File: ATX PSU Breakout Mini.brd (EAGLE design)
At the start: 100 x 99.8 mm, 43 parts, among them J1 ATX24RH, SW1 SW_PUSH_DPDT, T1 5V, T2 3V3, T3 12V, T4 GND, T5 ADJ, T6 -12V, U1 V_REG_317SINK, U2 TPS2513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

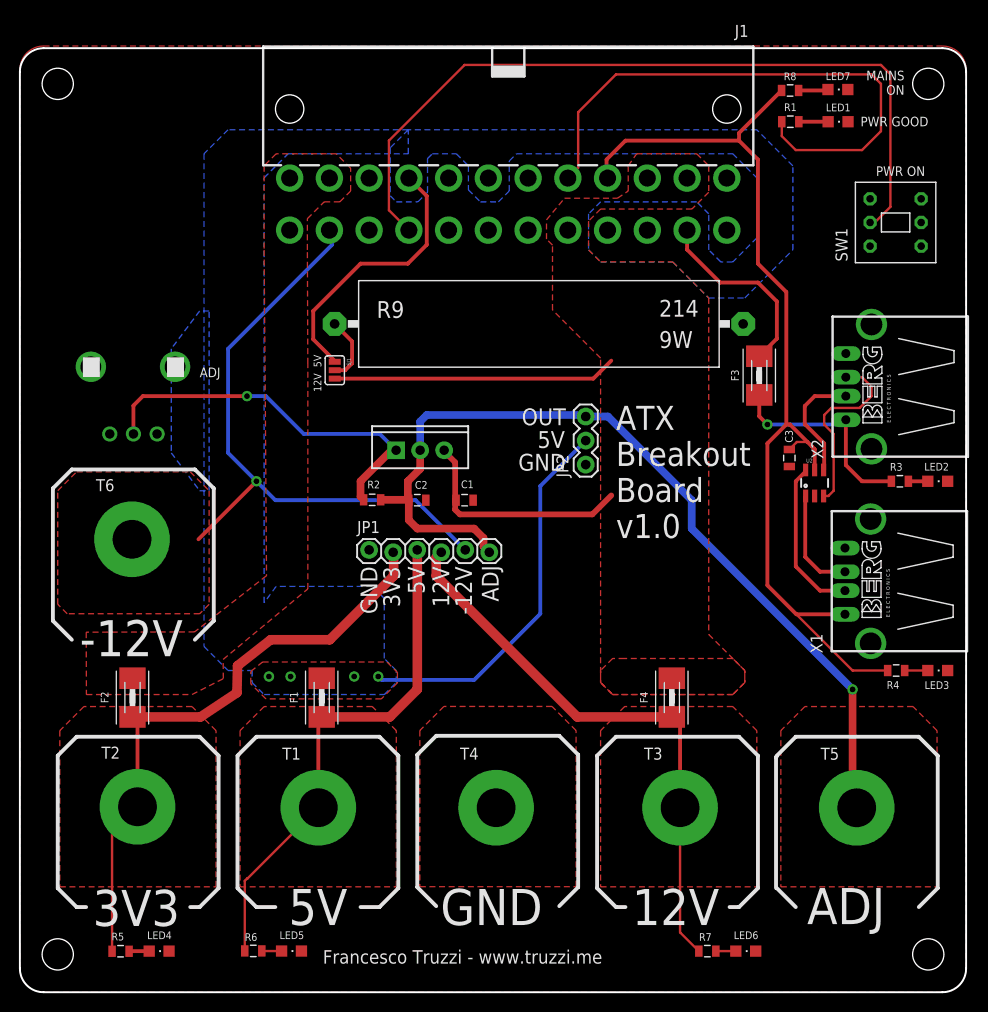
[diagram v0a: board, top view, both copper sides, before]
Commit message: Fixes and additions.
Thickened all traces, added resistors to the USB ports (you can use them
instead of the TPS2513)
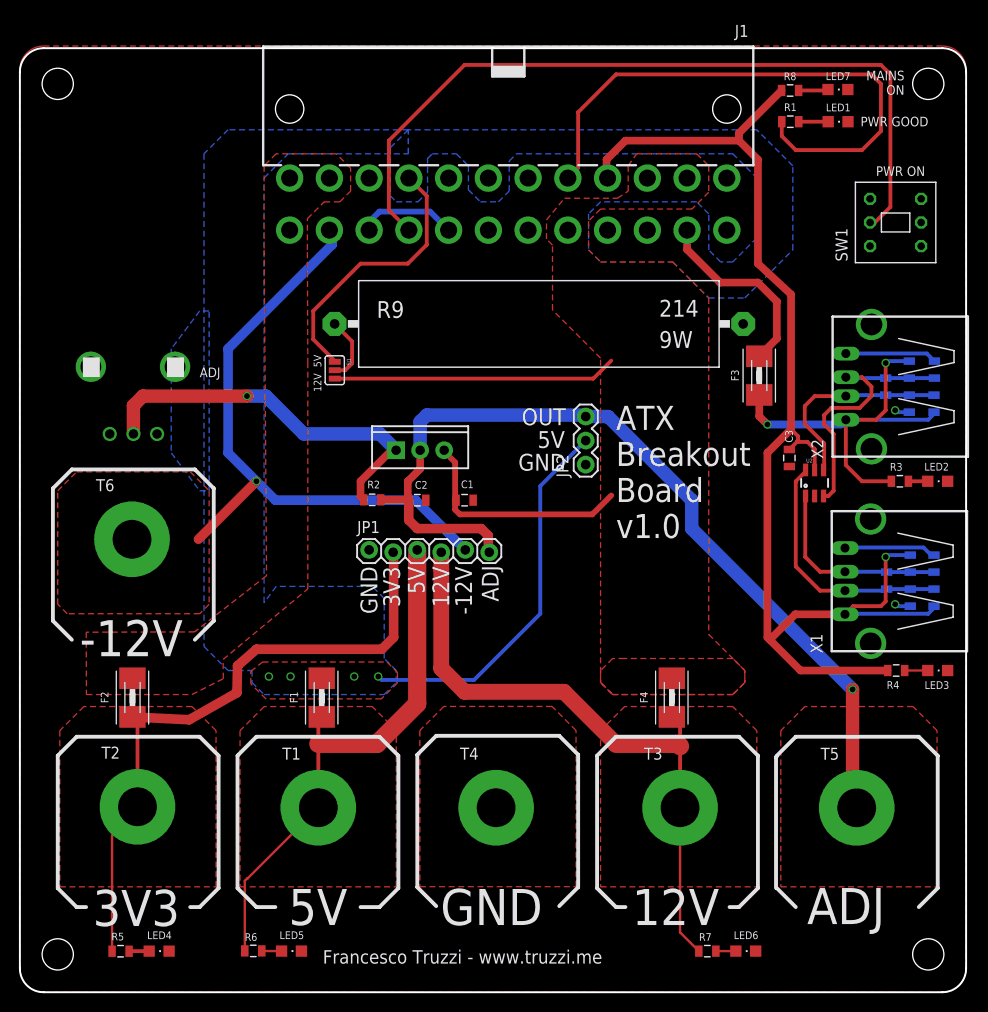
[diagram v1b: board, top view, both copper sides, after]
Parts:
- added R10, R15: (no value), SparkFun-Resistors:0805
- added R11, R16: 43K, SparkFun-Resistors:0805
- added R12, R14, R17, R19: 51K, SparkFun-Resistors:0805
- added R13, R18: 75K, SparkFun-Resistors:0805
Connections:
- net 5V_STDBY: now also R16.1, R18.1
- net DM1: now also R15.1, R16.2, R17.1
- net DM2: now also R10.1, R11.2, R12.1
- net DP1: now also R15.2, R18.2, R19.1
- net DP2: now also R10.2, R13.2, R14.1
- net GND: now also R12.2, R14.2, R17.2, R19.2
- net USB_P4: now also R11.1, R13.1
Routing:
- net GND: track 0.00 -> 33.2 mm, vias 0 -> 2
- net 5V_STDBY: track 104.0 -> 132.5 mm, vias 0 -> 1
- net USB_P4: track 22.3 -> 44.3 mm, vias 1 -> 2
- net DM1: track 16.9 -> 26.4 mm
- net DP1: track 11.3 -> 20.7 mm
- net DP2: track 19.7 -> 29.1 mm
- net DM2: track 12.4 -> 21.8 mm
- net 12VOUT: track 59.7 -> 66.9 mm
- net 3V3OUT: track 63.5 -> 67.4 mm
- net 5VOUT: track 54.2 -> 56.6 mm

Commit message: New version (v1.2)
Fixed bugs, rearranged traces and components, added pin headers, USB
resistors and prototyping area.
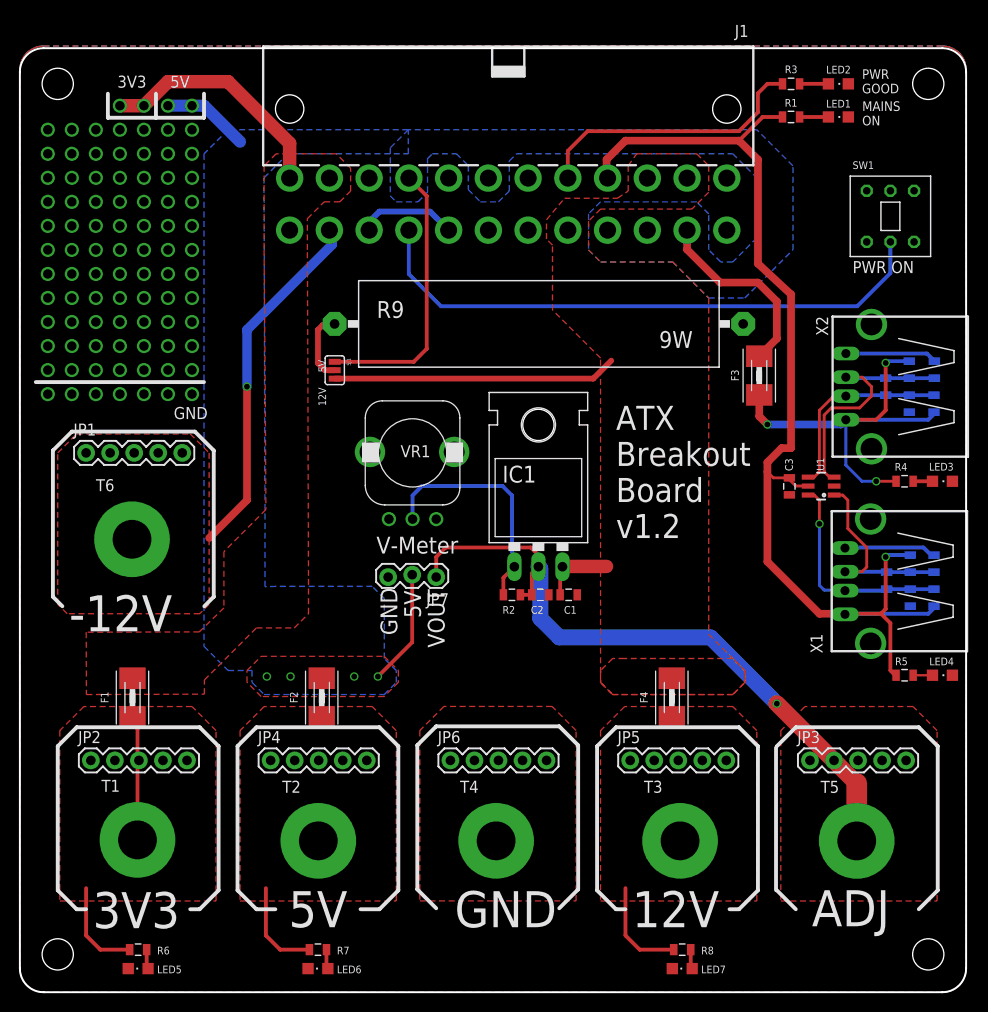
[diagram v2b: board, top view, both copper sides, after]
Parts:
- removed U2: TPS2513, SparkFun-DigitalIC:SOT23-6
- added IC1: (no value), v-reg:317TL
- added JP3, JP4, JP5, JP6: (no value), SparkFun-Connectors:1X05
- added JP7: (no value), SparkFun-Connectors:1X03_LOCK
- JP1: device SparkFun-Connectors:1X06_LOCK -> SparkFun-Connectors:1X05
- JP2: device SparkFun-Connectors:1X03 -> SparkFun-Connectors:1X05
- LED1: value GREEN -> RED
- LED2: value (none) -> GREEN
- LED7: value RED -> (none)
- R10, R15: value (none) -> 43K
- R11, R16: value 43K -> 75K
- R13, R18: value 75K -> (none)
- R3: value 1.2k -> 3.3k
- R6: value 3.3k -> 1.2k
- R7: value 10k -> 3.3k
- R8: value 3.3k -> 10k
- T1: value 5V -> 3V3
- T2: value 3V3 -> 5V
- U1: value V_REG_317SINK -> TPS2513; device SparkFun-PowerIC:TO220-ADJ -> SparkFun-DigitalIC:SOT23-6
- moved LED7 94.3 mm to (48.0, -31.5), turned to 90 degrees
- moved R8 91.5 mm to (48.0, -29.5)
- moved R5 87.8 mm to (71.5, -0.50)
- moved LED4 87.8 mm to (75.5, -0.50)
- moved JP2 60.9 mm to (-14.5, -9.50), turned to 0 degrees
- moved LED6 45.3 mm to (9.50, -31.5), turned to 90 degrees
- moved R3 43.5 mm to (59.5, 62.0)
- moved LED2 43.3 mm to (64.5, 62.0)
- moved U1 42.5 mm to (62.7, 19.5), turned to 90 degrees
- moved R7 41.2 mm to (9.50, -29.5)
- moved JP1 31.6 mm to (-15.0, 23.0)
- moved VR1 30.8 mm to (19.5, 20.0)
- moved R16 24.2 mm to (72.0, 31.8), turned to 270 degrees
- moved R10 22.9 mm to (74.6, 7.70)
- moved R13 22.4 mm to (69.6, 9.50), turned to 90 degrees
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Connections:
- net -12V: now also JP1.1, JP1.2, JP1.3, JP1.4
- net 12V: now also IC1.3; no longer U1.IN
- net 12VOUT: now also JP5.1, JP5.2, JP5.3, JP5.4, JP5.5, R8.1; no longer JP1.4, R7.1
- net 3V3: now also F1.2; no longer F2.2
- net 3V3OUT: now also F1.1, JP2.1, JP2.2, JP2.3, JP2.4, JP2.5, R6.1, T1.P; no longer F2.1, JP1.2, R5.1, T2.P
- net 5V: now also F2.2, JP7.2; no longer F1.2, JP2.2
- net 5VOUT: now also F2.1, JP4.1, JP4.2, JP4.3, JP4.4, JP4.5, R7.1, T2.P; no longer F1.1, JP1.3, R6.1, T1.P
- net 5V_STDBY: now also R1.1, R10.1, R11.1, R5.1, U1.5; no longer R16.1, R18.1, R4.1, R8.1, U2.5
- net DM1: now also R10.2, R12.1, R13.1, U1.6; no longer R15.1, R16.2, R17.1, U2.6
- net DM2: now also R15.2, R17.1, R18.1, U1.4; no longer R10.1, R11.2, R12.1, U2.4
- net DP1: now also R11.2, R13.2, R14.1, U1.1; no longer R15.2, R18.2, R19.1, U2.1
- net DP2: now also R16.2, R18.2, R19.1, U1.3; no longer R10.2, R13.2, R14.1, U2.3
- net GND: now also JP6.1, JP6.2, JP6.3, JP6.4, JP6.5, JP7.3, U1.2; no longer JP1.1, JP2.1, U2.2
- net N$1: now also R3.1; no longer R1.1
- net N$9: now also IC1.1; no longer U1.ADJ
- net USB_P4: now also R15.1, R16.1, R4.1; no longer R11.1, R13.1, R3.1
- net VOUT: now also IC1.2, JP3.1, JP3.2, JP3.3, JP3.4, JP3.5, JP7.1; no longer JP1.6, JP2.3, U1.OUT
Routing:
- net 12VOUT: track 66.9 -> 10.7 mm
- net 5VOUT: track 56.6 -> 10.2 mm
- net 3V3OUT: track 67.4 -> 23.4 mm
- net N$1: track 59.9 -> 29.7 mm
- net -12V: track 66.2 -> 38.0 mm
- net VOUT: track 97.4 -> 71.8 mm
- net 3V3: track 0.00 -> 25.4 mm, vias 0 -> 2
- net N$10: track 83.9 -> 61.7 mm
- net 5V: track 89.9 -> 70.9 mm, vias 4 -> 6
- net 12V: track 54.5 -> 37.8 mm
- net 5V_STDBY: track 132.5 -> 116.5 mm
- net N$9: track 40.8 -> 24.9 mm, vias 1 -> 0
- net DM1: track 26.4 -> 22.8 mm, vias 0 -> 1
- net GND: track 33.2 -> 30.0 mm, vias 2 -> 7
- net DP2: track 29.1 -> 26.6 mm
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- added copper zone on layer 16, net GND
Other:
- board text added: "ATX Breakout Board v1.2"
- board text added: "V-Meter"
- board text added: "VOUT"
- board text removed: "ATX Breakout Board v1.0"
- board text removed: "OUT"
